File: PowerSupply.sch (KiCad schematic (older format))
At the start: 0 parts

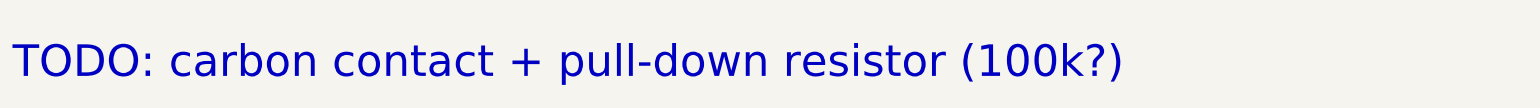
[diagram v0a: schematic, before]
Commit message: Add placeholder sheets for functions to be implemented
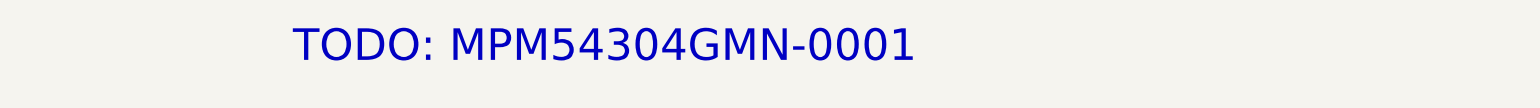
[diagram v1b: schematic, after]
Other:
- note added: "TODO: MPM54304GMN-0001"
- note removed: "TODO: carbon contact + pull-down resistor (100k?)"
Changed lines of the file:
@@
 $Descr A4 11693 8268
 encoding utf-8
-Sheet 10 16
-Title "Litter Robot 3 - Push button"
-Date "2021-02-28"
+Sheet 14 16
+Title "Litter Robot 3 - Power supply"
+Date "2021-03-02"
 Rev "A1"
 Comp "L. Sartory"
@@
 Comment4 ""
 $EndDescr
-Text Notes 2000 4100 0    197  ~ 0
-TODO: carbon contact + pull-down resistor (100k?)
+Text Notes 3750 4000 0    197  ~ 0
+TODO: MPM54304GMN-0001
 $EndSCHEMATC

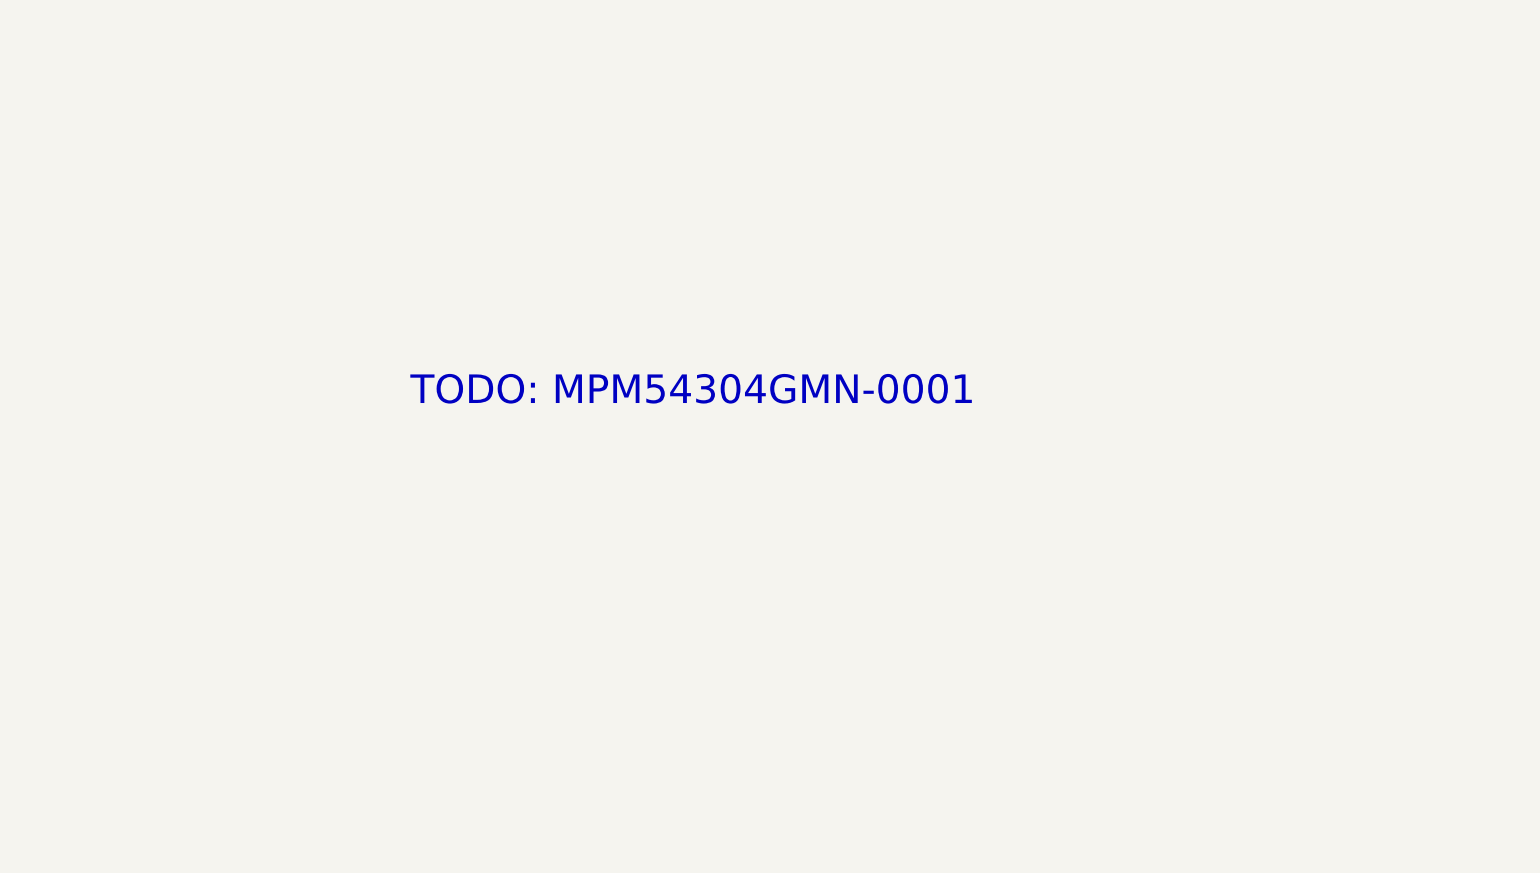
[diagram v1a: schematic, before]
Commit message: Add the power supply and motor driver ICs
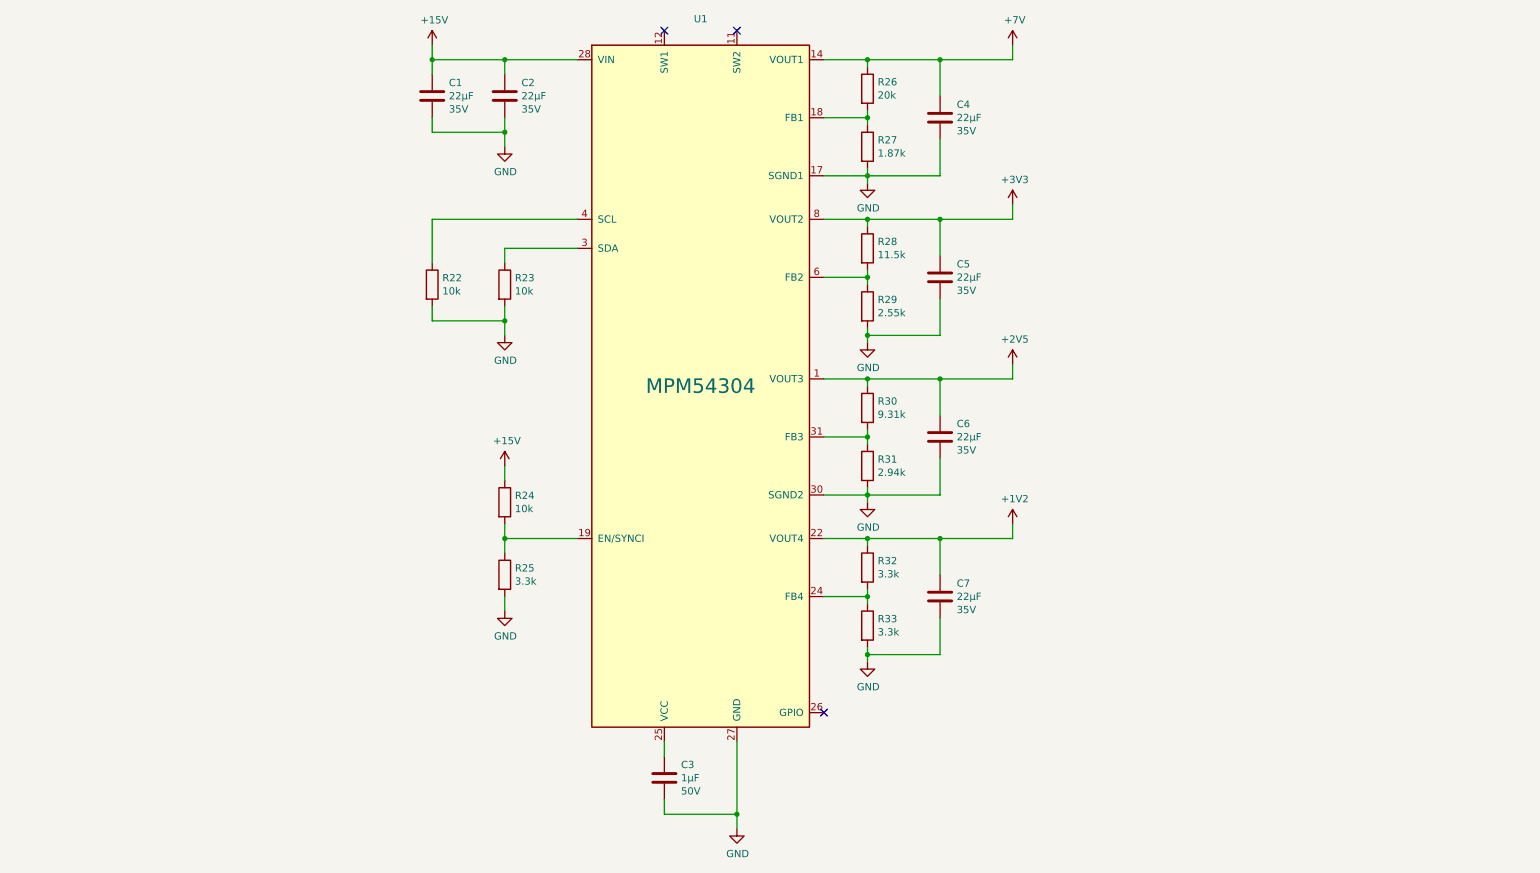
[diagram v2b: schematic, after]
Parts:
- added C1, C2, C4, C5, C6, C7: 22µF, Capacitor_SMD:C_0603_1608Metric, symbol Device:C
- added C3: 1µF, Capacitor_SMD:C_0603_1608Metric, symbol Device:C
- added R22, R23, R24: 10k, Resistor_SMD:R_0603_1608Metric, symbol Device:R
- added R25, R32, R33: 3.3k, Resistor_SMD:R_0603_1608Metric, symbol Device:R
- added R26: 20k, Resistor_SMD:R_0603_1608Metric, symbol Device:R
- added R27: 1.87k, Resistor_SMD:R_0603_1608Metric, symbol Device:R
- added R28: 11.5k, Resistor_SMD:R_0603_1608Metric, symbol Device:R
- added R29: 2.55k, Resistor_SMD:R_0603_1608Metric, symbol Device:R
- added R30: 9.31k, Resistor_SMD:R_0603_1608Metric, symbol Device:R
- added R31: 2.94k, Resistor_SMD:R_0603_1608Metric, symbol Device:R
- added U1: MPM54304, symbol LitterRobot:MPM54304
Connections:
- new net: R26.2, R27.1, U1.18 (FB1)
- new net: R24.2, R25.1, U1.19 (EN/SYNCI)
- new net: R32.2, R33.1, U1.24 (FB4)
- new net: C3.1, U1.25 (VCC)
- new net: R23.1, U1.3 (SDA)
- new net: R30.2, R31.1, U1.31 (FB3)
- new net: R22.1, U1.4 (SCL)
- new net: R28.2, R29.1, U1.6 (FB2)
- new net +15V: C1.1, C2.1, R24.1, U1.28 (VIN), U1.29 (VIN)
- new net +1V2: C7.1, R32.1, U1.22 (VOUT4), U1.23 (VOUT4)
- new net +2V5: C6.1, R30.1, U1.1 (VOUT3), U1.32 (VOUT3)
- new net +3V3: C5.1, R28.1, U1.8 (VOUT2), U1.9 (VOUT2)
- new net +7V: C4.1, R26.1, U1.14 (VOUT1), U1.15 (VOUT1)
- new net GND: C1.2, C2.2, C3.2, C4.2, C5.2, C6.2, C7.2, R22.2, R23.2, R25.2, R27.2, R29.2, R31.2, R33.2, U1.10 (GND), U1.13 (GND), U1.16 (GND), U1.17 (SGND1), U1.2 (GND), U1.20 (GND), U1.21 (GND), U1.27 (GND), U1.30 (SGND2), U1.33 (GND), U1.5 (GND), U1.7 (GND)
- no-connect marks 0 -> 3
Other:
- note removed: "TODO: MPM54304GMN-0001"

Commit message: Add the MPM54304 footprint
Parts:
- U1: footprint (none) -> LitterRobot:MPS_MPM54304_LGA33_7x7mm
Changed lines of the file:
@@
 F 0 "U1" H 5750 6381 50  0000 C CNN
 F 1 "MPM54304" H 5750 3850 100 0000 C CNN
-F 2 "" H 6300 6200 50  0001 C CNN
+F 2 "LitterRobot:MPS_MPM54304_LGA33_7x7mm" H 6300 6200 50  0001 C CNN
 F 3 "https://www.monolithicpower.com/en/documentview/productdocument/index/version/2/document_type/Datasheet/lang/en/sku/MPM54304/document_id/4982/" H 6300 6200 50  0001 C CNN
 F 4 "MPM54304GMN-0001" H 5750 3850 50  0001 C CNN "Part_Number"

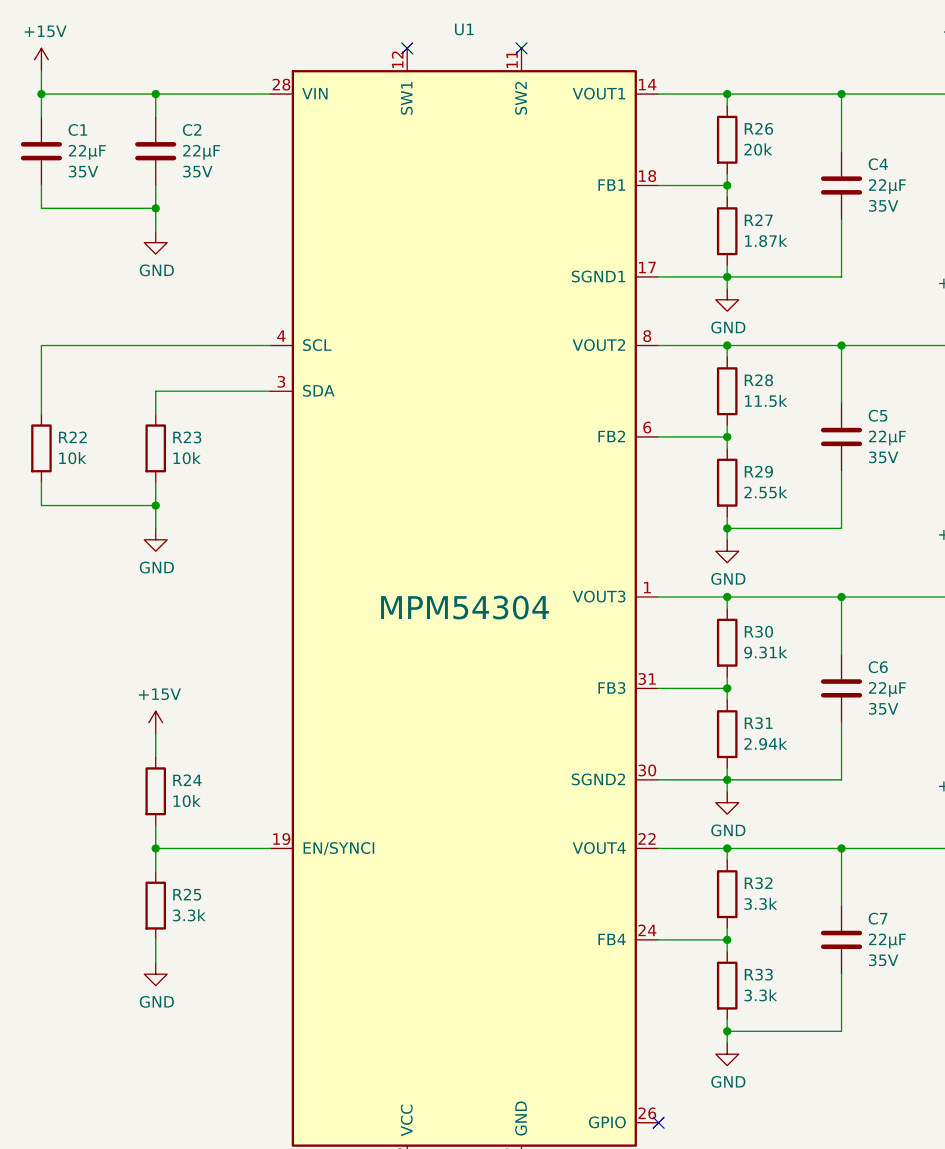
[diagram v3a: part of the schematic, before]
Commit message: Add the push buttons and mounting holes
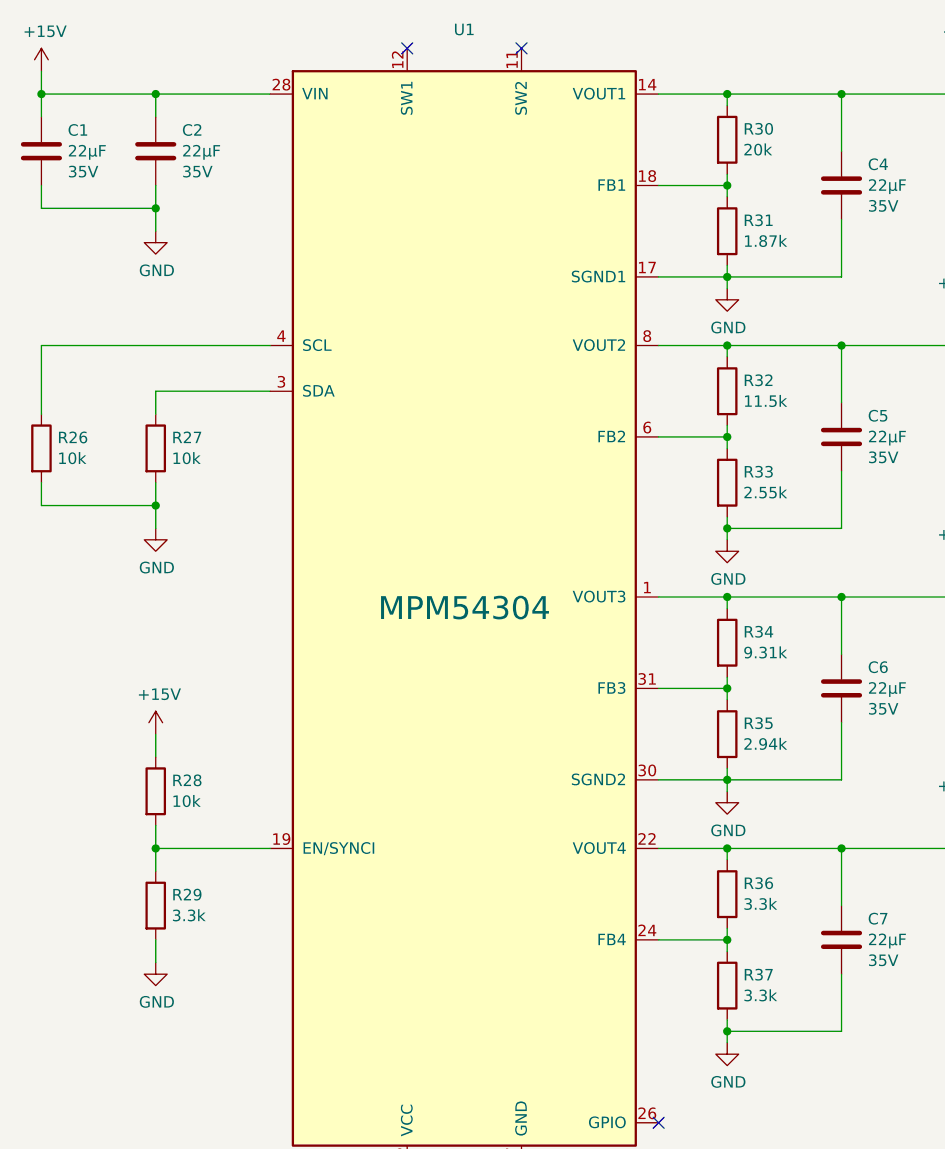
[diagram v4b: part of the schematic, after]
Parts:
- renumbered R22 to R26, R23 to R27, R24 to R28, R25 to R29, R26 to R30, R27 to R31, R28 to R32, R29 to R33, R30 to R34, R31 to R35, R32 to R36, R33 to R37
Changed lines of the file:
@@
 $EndComp
 $Comp
-L power:+15V #PWR037
+L power:+15V #PWR045
 U 1 1 6049C802
 P 3900 1500
-F 0 "#PWR037" H 3900 1350 50  0001 C CNN
+F 0 "#PWR045" H 3900 1350 50  0001 C CNN
 F 1 "+15V" H 3915 1673 50  0000 C CNN
 F 2 "" H 3900 1500 50  0001 C CNN
@@
 $EndComp
 $Comp
-L power:GND #PWR038
+L power:GND #PWR046
 U 1 1 604A0BB2
 P 4400 2200
-F 0 "#PWR038" H 4400 1950 50  0001 C CNN
+F 0 "#PWR046" H 4400 1950 50  0001 C CNN
 F 1 "GND" H 4405 2027 50  0000 C CNN
 F 2 "" H 4400 2200 50  0001 C CNN
@@
 P 4400 3150
 AR Path="/603F20AB/604A32A1" Ref="R?"  Part="1"
-AR Path="/603F1DCE/604A32A1" Ref="R23"  Part="1"
-F 0 "R23" H 4470 3196 50  0000 L CNN
+AR Path="/603F1DCE/604A32A1" Ref="R27"  Part="1"
+F 0 "R27" H 4470 3196 50  0000 L CNN
 F 1 "10k" H 4470 3105 50  0000 L CNN
 F 2 "Resistor_SMD:R_0603_1608Metric" V 4330 3150 50  0001 C CNN
@@
 P 3900 3150
 AR Path="/603F20AB/604A3347" Ref="R?"  Part="1"
-AR Path="/603F1DCE/604A3347" Ref="R22"  Part="1"
-F 0 "R22" H 3970 3196 50  0000 L CNN
+AR Path="/603F1DCE/604A3347" Ref="R26"  Part="1"
+F 0 "R26" H 3970 3196 50  0000 L CNN
 F 1 "10k" H 3970 3105 50  0000 L CNN
 F 2 "Resistor_SMD:R_0603_1608Metric" V 3830 3150 50  0001 C CNN
@@
 $EndComp
 $Comp
-L power:GND #PWR039
+L power:GND #PWR047
 U 1 1 604A378F
 P 4400 3500
-F 0 "#PWR039" H 4400 3250 50  0001 C CNN
+F 0 "#PWR047" H 4400 3250 50  0001 C CNN
 F 1 "GND" H 4405 3327 50  0000 C CNN
 F 2 "" H 4400 3500 50  0001 C CNN
@@
 P 4400 4650
 AR Path="/603F20AB/604A40DF" Ref="R?"  Part="1"
-AR Path="/603F1DCE/604A40DF" Ref="R24"  Part="1"
-F 0 "R24" H 4470 4696 50  0000 L CNN
+AR Path="/603F1DCE/604A40DF" Ref="R28"  Part="1"
+F 0 "R28" H 4470 4696 50  0000 L CNN
 F 1 "10k" H 4470 4605 50  0000 L CNN
 F 2 "Resistor_SMD:R_0603_1608Metric" V 4330 4650 50  0001 C CNN
@@
 P 4400 5150
 AR Path="/603F20AB/604A4902" Ref="R?"  Part="1"
-AR Path="/603F1DCE/604A4902" Ref="R25"  Part="1"
-F 0 "R25" H 4470 5196 50  0000 L CNN
+AR Path="/603F1DCE/604A4902" Ref="R29"  Part="1"
+F 0 "R29" H 4470 5196 50  0000 L CNN
 F 1 "3.3k" H 4470 5105 50  0000 L CNN
 F 2 "Resistor_SMD:R_0603_1608Metric" V 4330 5150 50  0001 C CNN
@@
 $EndComp
 $Comp
-L power:GND #PWR041
+L power:GND #PWR049
 U 1 1 604A4E38
 P 4400 5400
-F 0 "#PWR041" H 4400 5150 50  0001 C CNN
+F 0 "#PWR049" H 4400 5150 50  0001 C CNN
 F 1 "GND" H 4405 5227 50  0000 C CNN
 F 2 "" H 4400 5400 50  0001 C CNN
@@
 $EndComp
 $Comp
-L power:+15V #PWR040
+L power:+15V #PWR048
 U 1 1 604A52BA
 P 4400 4400
-F 0 "#PWR040" H 4400 4250 50  0001 C CNN
+F 0 "#PWR048" H 4400 4250 50  0001 C CNN
 F 1 "+15V" H 4415 4573 50  0000 C CNN
 F 2 "" H 4400 4400 50  0001 C CNN
@@
 $EndComp
 $Comp
-L power:GND #PWR042
+L power:GND #PWR050
 U 1 1 604AC677
 P 6000 6900
-F 0 "#PWR042" H 6000 6650 50  0001 C CNN
+F 0 "#PWR050" H 6000 6650 50  0001 C CNN
 F 1 "GND" H 6005 6727 50  0000 C CNN
 F 2 "" H 6000 6900 50  0001 C CNN
@@
 $EndComp
 $Comp
-L LitterRobot:+7V #PWR047
+L LitterRobot:+7V #PWR055
 U 1 1 604AE53B
 P 7900 1500
-F 0 "#PWR047" H 7900 1350 50  0001 C CNN
+F 0 "#PWR055" H 7900 1350 50  0001 C CNN
 F 1 "+7V" H 7915 1673 50  0000 C CNN
 F 2 "" H 7900 1500 50  0001 C CNN
@@
 $EndComp
 $Comp
-L power:+2V5 #PWR049
+L power:+2V5 #PWR057
 U 1 1 604B00EC
 P 7900 3700
-F 0 "#PWR049" H 7900 3550 50  0001 C CNN
+F 0 "#PWR057" H 7900 3550 50  0001 C CNN
 F 1 "+2V5" H 7915 3873 50  0000 C CNN
 F 2 "" H 7900 3700 50  0001 C CNN
@@
 $EndComp
 $Comp
-L power:+1V2 #PWR050
+L power:+1V2 #PWR058
 U 1 1 604B0B68
 P 7900 4800
-F 0 "#PWR050" H 7900 4650 50  0001 C CNN
+F 0 "#PWR058" H 7900 4650 50  0001 C CNN
 F 1 "+1V2" H 7915 4973 50  0000 C CNN
 F 2 "" H 7900 4800 50  0001 C CNN
@@
 P 6900 1800
 AR Path="/603F20AB/604B4786" Ref="R?"  Part="1"
-AR Path="/603F1DCE/604B4786" Ref="R26"  Part="1"
-F 0 "R26" H 6970 1846 50  0000 L CNN
+AR Path="/603F1DCE/604B4786" Ref="R30"  Part="1"
+F 0 "R30" H 6970 1846 50  0000 L CNN
 F 1 "20k" H 6970 1755 50  0000 L CNN
 F 2 "Resistor_SMD:R_0603_1608Metric" V 6830 1800 50  0001 C CNN
@@
 P 6900 2200
 AR Path="/603F20AB/604B542F" Ref="R?"  Part="1"
-AR Path="/603F1DCE/604B542F" Ref="R27"  Part="1"
-F 0 "R27" H 6970 2246 50  0000 L CNN
+AR Path="/603F1DCE/604B542F" Ref="R31"  Part="1"
+F 0 "R31" H 6970 2246 50  0000 L CNN
 F 1 "1.87k" H 6970 2155 50  0000 L CNN
 F 2 "Resistor_SMD:R_0603_1608Metric" V 6830 2200 50  0001 C CNN
@@
 $EndComp
 $Comp
-L power:GND #PWR043
+L power:GND #PWR051
 U 1 1 604B58A1
 P 6900 2450
-F 0 "#PWR043" H 6900 2200 50  0001 C CNN
+F 0 "#PWR051" H 6900 2200 50  0001 C CNN
 F 1 "GND" H 6905 2277 50  0000 C CNN
 F 2 "" H 6900 2450 50  0001 C CNN
@@
 P 6900 2900
 AR Path="/603F20AB/604CD95C" Ref="R?"  Part="1"
-AR Path="/603F1DCE/604CD95C" Ref="R28"  Part="1"
-F 0 "R28" H 6970 2946 50  0000 L CNN
+AR Path="/603F1DCE/604CD95C" Ref="R32"  Part="1"
+F 0 "R32" H 6970 2946 50  0000 L CNN
 F 1 "11.5k" H 6970 2855 50  0000 L CNN
 F 2 "Resistor_SMD:R_0603_1608Metric" V 6830 2900 50  0001 C CNN
@@
 P 6900 3300
 AR Path="/603F20AB/604CD963" Ref="R?"  Part="1"
-AR Path="/603F1DCE/604CD963" Ref="R29"  Part="1"
-F 0 "R29" H 6970 3346 50  0000 L CNN
+AR Path="/603F1DCE/604CD963" Ref="R33"  Part="1"
+F 0 "R33" H 6970 3346 50  0000 L CNN
 F 1 "2.55k" H 6970 3255 50  0000 L CNN
 F 2 "Resistor_SMD:R_0603_1608Metric" V 6830 3300 50  0001 C CNN
@@
 $EndComp
 $Comp
-L power:GND #PWR044
+L power:GND #PWR052
 U 1 1 604CD969
 P 6900 3550
-F 0 "#PWR044" H 6900 3300 50  0001 C CNN
+F 0 "#PWR052" H 6900 3300 50  0001 C CNN
 F 1 "GND" H 6905 3377 50  0000 C CNN
 F 2 "" H 6900 3550 50  0001 C CNN
@@
 P 6900 4000
 AR Path="/603F20AB/604D12FF" Ref="R?"  Part="1"
-AR Path="/603F1DCE/604D12FF" Ref="R30"  Part="1"
-F 0 "R30" H 6970 4046 50  0000 L CNN
+AR Path="/603F1DCE/604D12FF" Ref="R34"  Part="1"
+F 0 "R34" H 6970 4046 50  0000 L CNN
 F 1 "9.31k" H 6970 3955 50  0000 L CNN
 F 2 "Resistor_SMD:R_0603_1608Metric" V 6830 4000 50  0001 C CNN
@@
 P 6900 4400
 AR Path="/603F20AB/604D1306" Ref="R?"  Part="1"
-AR Path="/603F1DCE/604D1306" Ref="R31"  Part="1"
-F 0 "R31" H 6970 4446 50  0000 L CNN
+AR Path="/603F1DCE/604D1306" Ref="R35"  Part="1"
+F 0 "R35" H 6970 4446 50  0000 L CNN
 F 1 "2.94k" H 6970 4355 50  0000 L CNN
 F 2 "Resistor_SMD:R_0603_1608Metric" V 6830 4400 50  0001 C CNN
@@
 $EndComp
 $Comp
-L power:GND #PWR045
+L power:GND #PWR053
 U 1 1 604D130C
 P 6900 4650
-F 0 "#PWR045" H 6900 4400 50  0001 C CNN
+F 0 "#PWR053" H 6900 4400 50  0001 C CNN
 F 1 "GND" H 6905 4477 50  0000 C CNN
 F 2 "" H 6900 4650 50  0001 C CNN
@@
 	7900 4900 7400 4900
 $Comp
-L power:GND #PWR046
+L power:GND #PWR054
 U 1 1 604D31B7
 P 6900 5750
-F 0 "#PWR046" H 6900 5500 50  0001 C CNN
+F 0 "#PWR054" H 6900 5500 50  0001 C CNN
 F 1 "GND" H 6905 5577 50  0000 C CNN
 F 2 "" H 6900 5750 50  0001 C CNN
@@
 	4400 1600 4900 1600
 $Comp
-L power:+3V3 #PWR048
+L power:+3V3 #PWR056
 U 1 1 604F7C44
 P 7900 2600
-F 0 "#PWR048" H 7900 2450 50  0001 C CNN
+F 0 "#PWR056" H 7900 2450 50  0001 C CNN
 F 1 "+3V3" H 7915 2773 50  0000 C CNN
 F 2 "" H 7900 2600 50  0001 C CNN
@@
 P 6900 5100
 AR Path="/603F20AB/604FA5AF" Ref="R?"  Part="1"
-AR Path="/603F1DCE/604FA5AF" Ref="R32"  Part="1"
-F 0 "R32" H 6970 5146 50  0000 L CNN
+AR Path="/603F1DCE/604FA5AF" Ref="R36"  Part="1"
+F 0 "R36" H 6970 5146 50  0000 L CNN
 F 1 "3.3k" H 6970 5055 50  0000 L CNN
 F 2 "Resistor_SMD:R_0603_1608Metric" V 6830 5100 50  0001 C CNN
@@
 P 6900 5500
 AR Path="/603F20AB/604FB145" Ref="R?"  Part="1"
-AR Path="/603F1DCE/604FB145" Ref="R33"  Part="1"
-F 0 "R33" H 6970 5546 50  0000 L CNN
+AR Path="/603F1DCE/604FB145" Ref="R37"  Part="1"
+F 0 "R37" H 6970 5546 50  0000 L CNN
 F 1 "3.3k" H 6970 5455 50  0000 L CNN
 F 2 "Resistor_SMD:R_0603_1608Metric" V 6830 5500 50  0001 C CNN

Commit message: Add TODO notes
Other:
- note added: "TODO:\nPower good (GPIO)\n→ FPGA reset"
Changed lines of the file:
@@
 	1    0    0    -1
 $EndComp
+Text Notes 1000 6550 0    197  ~ 0
+TODO:\nPower good (GPIO)\n→ FPGA reset
 $EndSCHEMATC

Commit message: Add fuse and more inter-page signals
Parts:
- added R39: 10k, Resistor_SMD:R_0603_1608Metric, symbol Device:R
- renumbered C7 to C10, C1 to C4, C2 to C5, C3 to C6, C4 to C7, C5 to C8, C6 to C9, R26 to R27, R27 to R28, R28 to R29, R29 to R30, R30 to R31, R31 to R32, R32 to R33, R33 to R34, R34 to R35, R35 to R36, R36 to R37, R37 to R38, U1 to U2
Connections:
- net +3V3: now also R39.1
- net Power_good: now reaches U2.26 (GPIO)
- net Power_good: now also R39.2
- no-connect marks 3 -> 2
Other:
- note removed: "TODO:\nPower good (GPIO)\n→ FPGA reset"
